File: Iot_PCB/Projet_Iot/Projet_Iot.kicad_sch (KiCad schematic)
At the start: 13 parts, among them U6 uPesy_ESP32_Wroom_Low_Power_D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

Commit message: fix(kicad) : update with the latest files
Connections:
- net Lora/LoraRx: now also U6.25 (GPIO17); no longer U6.26 (GPIO16)
- net Lora/LoraTx: now also U6.26 (GPIO16); no longer U6.25 (GPIO17)

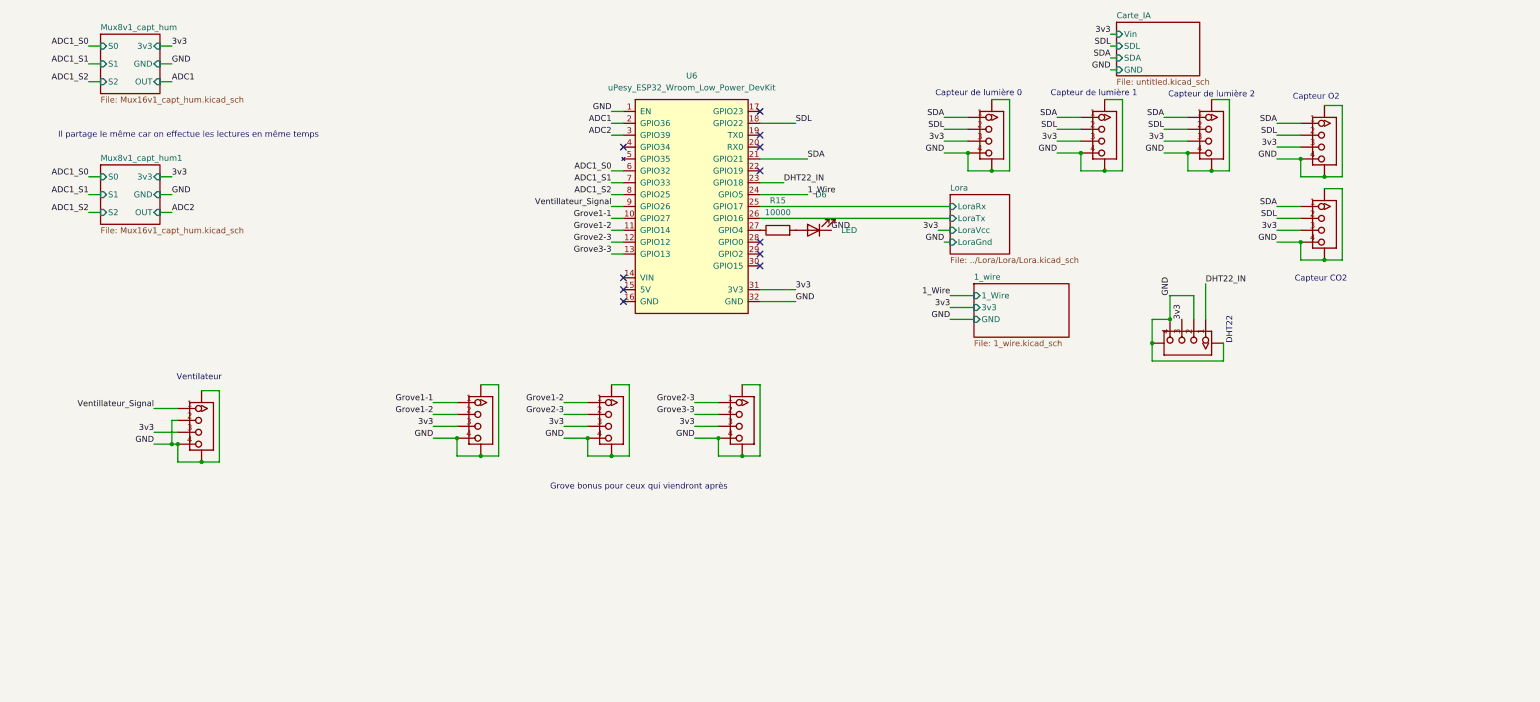
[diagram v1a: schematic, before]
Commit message: remplacement des grove lora par des vrais
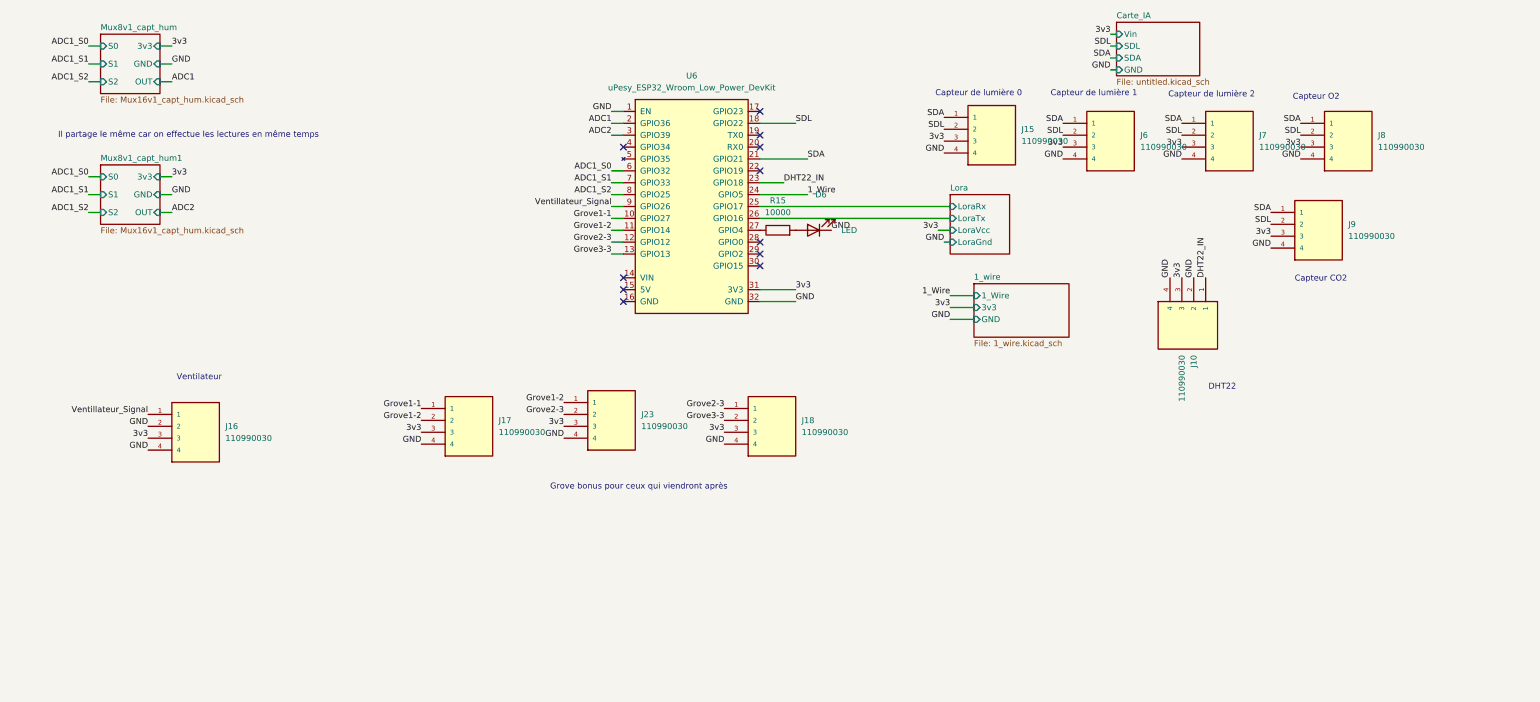
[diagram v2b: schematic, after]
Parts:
- removed J10, J23, J40, J41, J42, J43, J6, J7, J8, J9: ~, Lora:HW4-SMD-2.0, symbol Lora-eagle-import:GROVE-CONNECTOR-SMD'DD'
- added J10, J15, J16, J17, J18, J23, J6, J7, J8, J9: 110990030, 110990030:SEEED_110990030, symbol grove:110990030
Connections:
- net 3v3: now also J10.3, J15.3, J16.3, J17.3, J18.3, J23.3, J6.3, J7.3, J8.3, J9.3
- net DHT22_IN: now also J10.1
- net GND: now also J10.2, J10.4, J15.4, J16.2, J16.4, J17.4, J18.4, J23.4, J6.4, J7.4, J8.4, J9.4
- net Grove1-1: now also J17.1
- net Grove1-2: now also J17.2, J23.1
- net Grove2-3: now also J18.1, J23.2
- net Grove3-3: now also J18.2
- net SDA: now also J15.1, J6.1, J7.1, J8.1, J9.1
- net SDL: now also J15.2, J6.2, J7.2, J8.2, J9.2
- net Ventillateur_Signal: now also J16.1

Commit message: update 1-wire, pull_up i2c, switch load added but not configured yet (wait for test)
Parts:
- added R16: R, symbol Device:R
- added U11: FDC6326L, FDC6326L:SOT95P280X110-6N, symbol switch_load:FDC6326L
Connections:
- net 3v3: now also R16.1
- net SDA: now also R16.2
- no-connect marks 11 -> 17
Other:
- note added: "Pull_up I2C"

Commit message: adding grove to replace lora
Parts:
- added J24: 110990030, 110990030:SEEED_110990030, symbol grove:110990030
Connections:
- net 3v3: now also J24.3
- net GND: now also J24.4
- net Lora/LoraRx: no longer names the net of U6.25 (GPIO17)
- net Lora/LoraRx: now also J24.1
- net Lora/LoraTx: no longer names the net of U6.26 (GPIO16)
- net Lora/LoraTx: now also J24.2
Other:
- removed sheet Lora
- note added: "Lora"
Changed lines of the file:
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@@
 		)
 	)
+	(text "Lora"
+		(exclude_from_sim no)
+		(at 203.962 39.37 0)
+		(effects
+			(font
+				(size 1.27 1.27)
+			)
+		)
+	)
 	(text "Capteur de lumière 1"
 		(exclude_from_sim no)
@@
 	(symbol
 		(lib_id "grove:110990030")
+		(at 207.01 45.72 0)
+		(unit 1)
+		(exclude_from_sim no)
+		(in_bom yes)
+		(on_board yes)
+		(dnp no)
+		(fields_autoplaced yes)
+		(property "Reference" "J24"
+			(at 213.36 45.7199 0)
+			(effects
+				(font
+					(size 1.27 1.27)
+				)
+				(justify left)
+			)
+		)
+		(property "Value" "110990030"
+			(at 213.36 48.2599 0)
+			(effects
+				(font
+					(size 1.27 1.27)
+				)
+				(justify left)
+			)
+		)
+		(property "Footprint" "110990030:SEEED_110990030"
+			(at 207.01 45.72 0)
+			(effects
+				(font
+					(size 1.27 1.27)
+				)
+				(justify bottom)
+				(hide yes)
+			)
+		)
+		(property "Datasheet" ""
+			(at 207.01 45.72 0)
+			(effects
+				(font
+					(size 1.27 1.27)
+				)
+				(hide yes)
+			)
+		)
+		(property "Description" ""
+			(at 207.01 45.72 0)
+			(effects
+				(font
+					(size 1.27 1.27)
+				)
+				(hide yes)
+			)
+		)
+		(property "MF" "Seeed Technology Co., Ltd"
+			(at 207.01 45.72 0)
+			(effects
+				(font
+					(size 1.27 1.27)
+				)
+				(justify bottom)
+				(hide yes)
+			)
+		)
+		(property "MAXIMUM_PACKAGE_HEIGHT" "8.1mm"
+			(at 207.01 45.72 0)
+			(effects
+				(font
+					(size 1.27 1.27)
+				)
+				(justify bottom)
+				(hide yes)
+			)
+		)
+		(property "Package" "None"
+			(at 207.01 45.72 0)
+			(effects
+				(font
+					(size 1.27 1.27)
+				)
+				(justify bottom)
+				(hide yes)
+			)
+		)
+		(property "Price" "None"
+			(at 207.01 45.72 0)
+			(effects
+				(font
+					(size 1.27 1.27)
+				)
+				(justify bottom)
+				(hide yes)
+			)
+		)
+		(property "Check_prices" "https://www.snapeda.com/parts/110990030/Seeed+Studio/view-part/?ref=eda"
+			(at 207.01 45.72 0)
+			(effects
+				(font
+					(size 1.27 1.27)
+				)
+				(justify bottom)
+				(hide yes)
+			)
+		)
+		(property "STANDARD" "Manufacturer Recommendations"
+			(at 207.01 45.72 0)
+			(effects
+				(font
+					(size 1.27 1.27)
+				)
+				(justify bottom)
+				(hide yes)
+			)
+		)
+		(property "PARTREV" "A"
+			(at 207.01 45.72 0)
+			(effects
+				(font
+					(size 1.27 1.27)
+				)
+				(justify bottom)
+				(hide yes)
+			)
+		)
+		(property "SnapEDA_Link" "https://www.snapeda.com/parts/110990030/Seeed+Studio/view-part/?ref=snap"
+			(at 207.01 45.72 0)
+			(effects
+				(font
+					(size 1.27 1.27)
+				)
+				(justify bottom)
+				(hide yes)
+			)
+		)
+		(property "MP" "110990030"
+			(at 207.01 45.72 0)
+			(effects
+				(font
+					(size 1.27 1.27)
+				)
+				(justify bottom)
+				(hide yes)
+			)
+		)
+		(property "Description_1" "\n                        \n                            GROVE 2MM 4PIN VERT CONN 10PCS\n                        \n"
+			(at 207.01 45.72 0)
+			(effects
+				(font
+					(size 1.27 1.27)
+				)
+				(justify bottom)
+				(hide yes)
+			)
+		)
+		(property "Availability" "In Stock"
+			(at 207.01 45.72 0)
+			(effects
+				(font
+					(size 1.27 1.27)
+				)
+				(justify bottom)
+				(hide yes)
+			)
+		)
+		(property "MANUFACTURER" "Seeed Technology"
+			(at 207.01 45.72 0)
+			(effects
+				(font
+					(size 1.27 1.27)
+				)
+				(justify bottom)
+				(hide yes)
+			)
+		)
+		(pin "2"
+		)
+		(pin "1"
+		)
+		(pin "4"
+		)
+		(pin "3"
+		)
+		(instances
+			(project "Projet_Iot"
+				(path "/1ed8458c-022b-42bb-9785-a8267003d72a"
+					(reference "J24")
+					(unit 1)
+				)
+			)
+		)
+	)
+	(symbol
+		(lib_id "grove:110990030")
 		(at 248.92 68.58 270)
 		(unit 1)
@@
 				)
 			)
-		)
-	)
-	(sheet
-		(at 196.85 40.64)
-		(size 12.7 12.7)
-		(fields_autoplaced yes)
-		(stroke
-			(width 0.1524)
-			(type solid)
-			(color 0 0 0 1)
-		)
-		(fill
-			(color 80 186 219 1.0000)
-		)
-		(property "Sheetname" "Lora"
-			(at 196.85 39.9284 0)
-			(effects
-				(font
-					(size 1.27 1.27)
-				)
-				(justify left bottom)
-			)
-		)
-		(property "Sheetfile" "../Lora/Lora/Lora.kicad_sch"
-			(at 196.85 53.9246 0)
-			(effects
-				(font
-					(size 1.27 1.27)
-				)
-				(justify left top)
-				(hide yes)
-			)
-		)
-		(pin "LoraGnd" input
-			(at 196.85 50.8 180)
-			(effects
-				(font
-					(size 1.27 1.27)
-				)
-				(justify left)
-			)
-		)
-		(pin "LoraTx" input
-			(at 196.85 45.72 180)
-			(effects
-				(font
-					(size 1.27 1.27)
-				)
-				(justify left)
-			)
-		)
-		(pin "LoraVcc" input
-			(at 196.85 48.26 180)
-			(effects
-				(font
-					(size 1.27 1.27)
-				)
-				(justify left)
-			)
-		)
-		(pin "LoraRx" input
-			(at 196.85 43.18 180)
-			(effects
-				(font
-					(size 1.27 1.27)
-				)
-				(justify left)
-			)
-		)
-		(instances
-			(project "Projet_Iot"
-				(path "/1ed8458c-022b-42bb-9785-a8267003d72a"
-					(page "3")
-				)
-			)

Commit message: build(kicad): add a trace to every schematic
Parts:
- D6: footprint (none) -> LED_THT:LED_D5.0mm
- R15, R16: footprint (none) -> Resistor_THT:R_Axial_DIN0207_L6.3mm_D2.5mm_P10.16mm_Horizontal

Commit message: build(kicad) : start PCB
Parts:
- J10, J15, J16, J17, J18, J23, J24, J6, J7, J8, J9: footprint 110990030:SEEED_110990030 -> Grove:SEEED_110990030
- U6: footprint uPesy:uPesy_ESP32_Wroom_Low_Power_DevKit -> uPesyBoards:uPesy_ESP32_Wroom_Low_Power_DevKit
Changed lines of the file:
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@@
 			)
 		)
-		(property "Footprint" "110990030:SEEED_110990030"
+		(property "Footprint" "Grove:SEEED_110990030"
 			(at 93.98 88.9 0)
 			(effects
@@
 			)
 		)
-		(property "Footprint" "uPesy:uPesy_ESP32_Wroom_Low_Power_DevKit"
+		(property "Footprint" "uPesyBoards:uPesy_ESP32_Wroom_Low_Power_DevKit"
 			(at 139.7 17.78 0)
 			(effects
@@
 			)
 		)
-		(property "Footprint" "110990030:SEEED_110990030"
+		(property "Footprint" "Grove:SEEED_110990030"
 			(at 205.74 26.67 0)
 			(effects
@@
 			)
 		)
-		(property "Footprint" "110990030:SEEED_110990030"
+		(property "Footprint" "Grove:SEEED_110990030"
 			(at 256.54 27.94 0)
 			(effects
@@
 			)
 		)
-		(property "Footprint" "110990030:SEEED_110990030"
+		(property "Footprint" "Grove:SEEED_110990030"
 			(at 207.01 45.72 0)
 			(effects
@@
 			)
 		)
-		(property "Footprint" "110990030:SEEED_110990030"
+		(property "Footprint" "Grove:SEEED_110990030"
 			(at 248.92 68.58 0)
 			(effects
@@
 			)
 		)
-		(property "Footprint" "110990030:SEEED_110990030"
+		(property "Footprint" "Grove:SEEED_110990030"
 			(at 35.56 90.17 0)
 			(effects
@@
 			)
 		)
-		(property "Footprint" "110990030:SEEED_110990030"
+		(property "Footprint" "Grove:SEEED_110990030"
 			(at 275.59 46.99 0)
 			(effects
@@
 			)
 		)
-		(property "Footprint" "110990030:SEEED_110990030"
+		(property "Footprint" "Grove:SEEED_110990030"
 			(at 124.46 87.63 0)
 			(effects
@@
 			)
 		)
-		(property "Footprint" "110990030:SEEED_110990030"
+		(property "Footprint" "Grove:SEEED_110990030"
 			(at 231.14 27.94 0)
 			(effects
@@
 			)
 		)
-		(property "Footprint" "110990030:SEEED_110990030"
+		(property "Footprint" "Grove:SEEED_110990030"
 			(at 158.75 88.9 0)
 			(effects
@@
 			)
 		)
-		(property "Footprint" "110990030:SEEED_110990030"
+		(property "Footprint" "Grove:SEEED_110990030"
 			(at 281.94 27.94 0)
 			(effects

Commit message: pcb mis à jour
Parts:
- added C6: C, symbol Device:C
- added R6: 1000, symbol Device:R
- added R7: 100, symbol Device:R
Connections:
- net 3v3: now also U11.2 (VOUT,C1_2), C6.2; no longer U6.31 (3V3)
- net GND: now also R7.1; no longer U6.1 (EN)
- net Enable_LS: now reaches U6.30 (GPIO15)
- net Enable_LS: now also U11.6 (R1,C1)
- net at U11.1 (R2): now also R7.2
- net 3v3_ESP: now reaches U11.4 (VIN,R1)
- net 3v3_ESP: now also U6.31 (3V3), R6.2
- net at U11.5 (ON/OFF): now also C6.1, R6.1
- no-connect marks 17 -> 12
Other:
- moved on the sheet: U11

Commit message: pcb and schematic up to date
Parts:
- removed J10, J7, J8, J9: 110990030, Grove:SEEED_110990030, symbol grove:110990030
- removed R16: R, Resistor_THT:R_Axial_DIN0207_L6.3mm_D2.5mm_P10.16mm_Horizontal, symbol Device:R
- added J7: Conn_01x04_Pin, symbol Connector:Conn_01x04_Pin
- added R10: 4700, symbol Device:R
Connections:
- net 1_Wire: now also J6.1
- net Enable_LS: now also U11.5 (ON/OFF), R10.1; no longer U11.6 (R1,C1)
- net GND: now also C6.1, R10.2; no longer J16.2
- net SDA: now also J16.1; no longer J6.1
- net SDL: now also J16.2; no longer J6.2
- net interrupt_ia: now reaches U6.22 (GPIO19)
- net ADC2: no longer names the net of U6.3 (GPIO39)
- net Ventillateur_Signal: no longer names the net of U6.9 (GPIO26)
- net Ventillateur_Signal: no longer J16.1
- new net: R6.1, U11.6 (R1,C1)
- new net ventillateur_commande/12v: J7.2 (Pin_2)
- new net ventillateur_commande/GND_vent: J7.1 (Pin_1)
- new net ventillateur_commande/PWM: J7.3 (Pin_3)
- new net ventillateur_commande/TACH: J7.4 (Pin_4)
- no-connect marks 12 -> 15
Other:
- removed sheet 1_wire
- removed sheet Mux8v1_capt_hum1
- added sheet ventillateur_commande (ventillateur_compmande.kicad_sch)
- sheet Carte_IA ports: added interrupt_ia; removed none
- note added: "1_wire"
- note added: "Capteur de lumière / c02 / o2"
- note removed: "Capteur CO2"
- note removed: "Capteur O2"
- note removed: "Capteur de lumière 0"
- note removed: "Capteur de lumière 1"
- note removed: "Capteur de lumière 2"
- note removed: "DHT22"
- note removed: "Il partage le même car on effectue les lectures en même temps"
- note removed: "Pull_up I2C"
- moved on the sheet: C6, J15, J16, J17, J18, J23, R6, R7, U11
